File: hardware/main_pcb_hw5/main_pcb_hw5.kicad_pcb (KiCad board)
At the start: 2 copper layers, 100 x 77 mm, 24 parts, among them J1 MEGA TOP, J2 MEGA BOTTOM, J3 CART SLOT TOP ROW, J4 CART SLOT BOTTOM ROW, J5 MEGA SIDE, J6 5V USB, J7 Conn_01x07, J8 EXP2, J9 EXP1, M2_3 Screw_Terminal_01x01, M2_4 Screw_Terminal_01x01, M2_5 Screw_Terminal_01x01, M2_6 Screw_Terminal_01x01, M2_7 Screw_Terminal_01x01, M2_8 Screw_Terminal_01x01, M2_9 Screw_Terminal_01x01, SW1 VOLTAGE, SW2 POWER

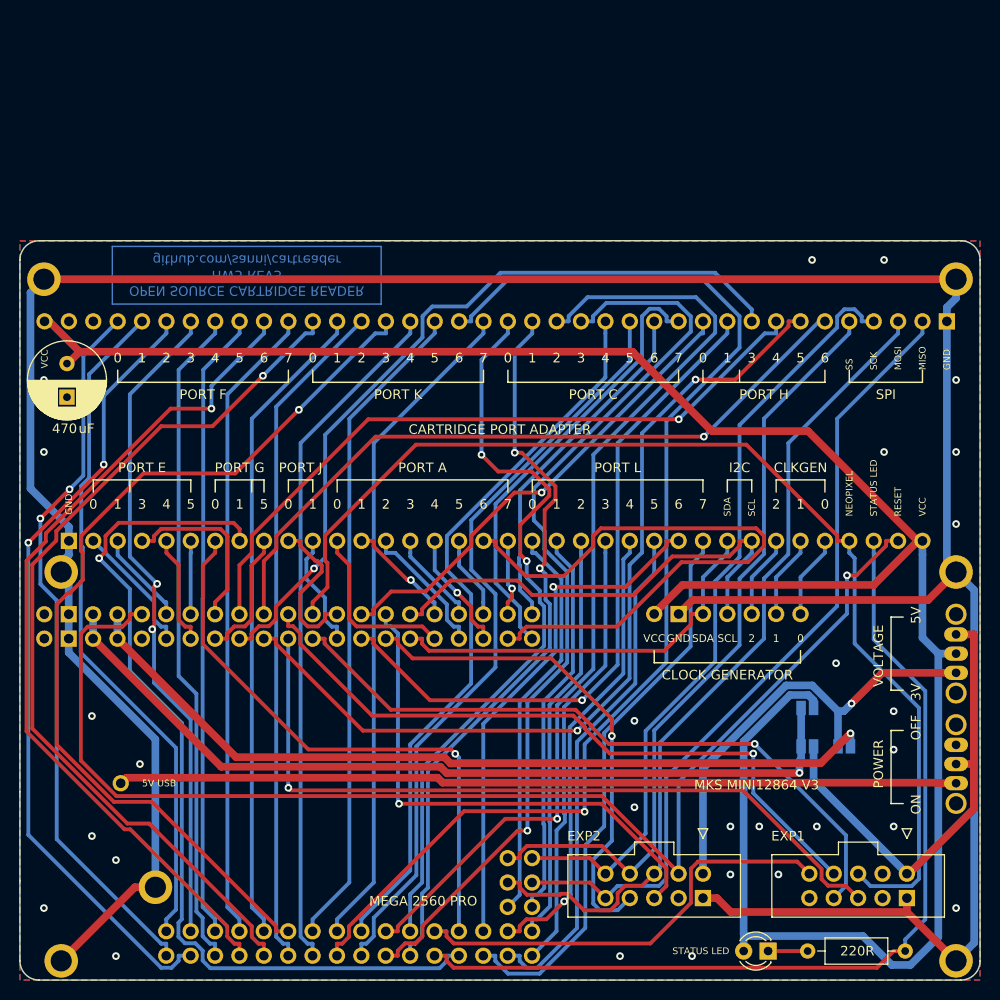
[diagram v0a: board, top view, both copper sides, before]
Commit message: Move main PCB updates to clean branch
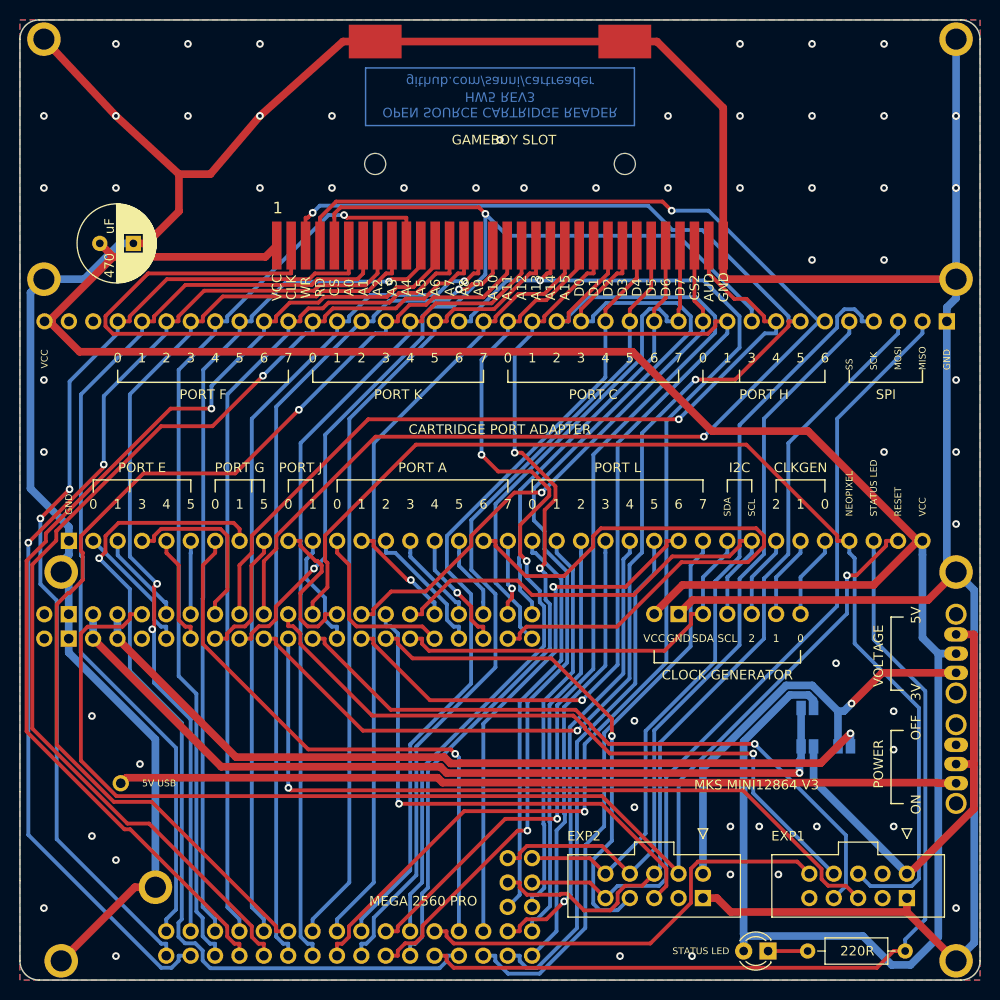
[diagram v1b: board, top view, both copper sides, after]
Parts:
- added J10: GBA_Slot, !OSCR:GBA_Slot, F.Cu at (150.0, 68.5)
- added M2_1: Screw_Terminal_01x01, MountingHole:MountingHole_2.2mm_M2_ISO7380_Pad, F.Cu at (102.5, 52.0)
- added M2_2: Screw_Terminal_01x01, MountingHole:MountingHole_2.2mm_M2_ISO7380_Pad, F.Cu at (197.5, 52.0)
- moved C1 13.0 mm to (108.3, 73.3), turned to 0 degrees
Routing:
- net D16: track 71.7 -> 162.7 mm
- net GND: track 312.5 -> 390.5 mm, vias 28 -> 58
- net D9: track 75.1 -> 135.9 mm, vias 1 -> 2
- net D8: track 92.3 -> 152.6 mm, vias 2 -> 3
- net A0: track 75.1 -> 104.5 mm
- net D6: track 81.8 -> 110.2 mm, vias 1 -> 2
- net A1: track 70.8 -> 99.2 mm
- net A4: track 69.5 -> 97.3 mm, vias 0 -> 1
- net VCC: track 231.8 -> 259.2 mm
- net A2: track 82.9 -> 110.2 mm
- net A3: track 69.2 -> 95.4 mm
- net A5: track 65.7 -> 89.3 mm, vias 0 -> 1
- net A6: track 88.6 -> 111.3 mm
- net A7: track 66.7 -> 88.7 mm
- net A8: track 93.4 -> 114.4 mm
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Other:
- board size 100 x 77 mm -> 100 x 100 mm
- board text added: "AUD"
- board text added: "CLK"
- board text added: "CS"
- board text added: "CS2"
- board text added: "GAMEBOY SLOT"
- board text added: "RD"
- board text added: "WR"
